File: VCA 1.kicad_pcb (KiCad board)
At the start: 2 copper layers, 171.3 x 128.5 mm, 89 parts, among them J1 Eurorack 2x8hs, J10 CV2, J11 IN2, J12 IN 1x8h, J13 OUT1, J14 OUT2, J15 IN 1x8s, J2 OUT 1x3s, J3 CV 1x9s, J5 CV 1x9h, J6 OUT 1x3h, J8 CV1, J9 IN1, Q1 2N3904, Q2 2N3904, U1 TL074, U2 AS2164

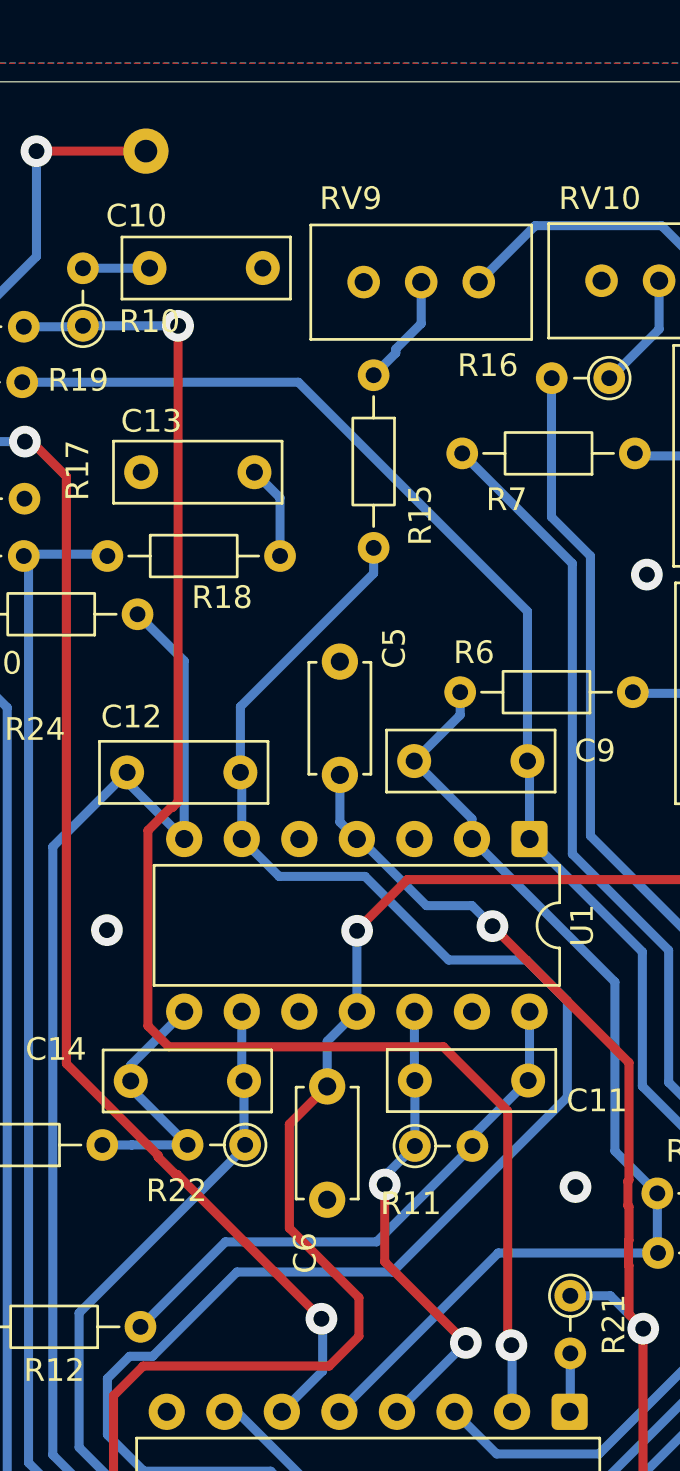
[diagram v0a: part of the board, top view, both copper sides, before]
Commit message: Added missing GND vias
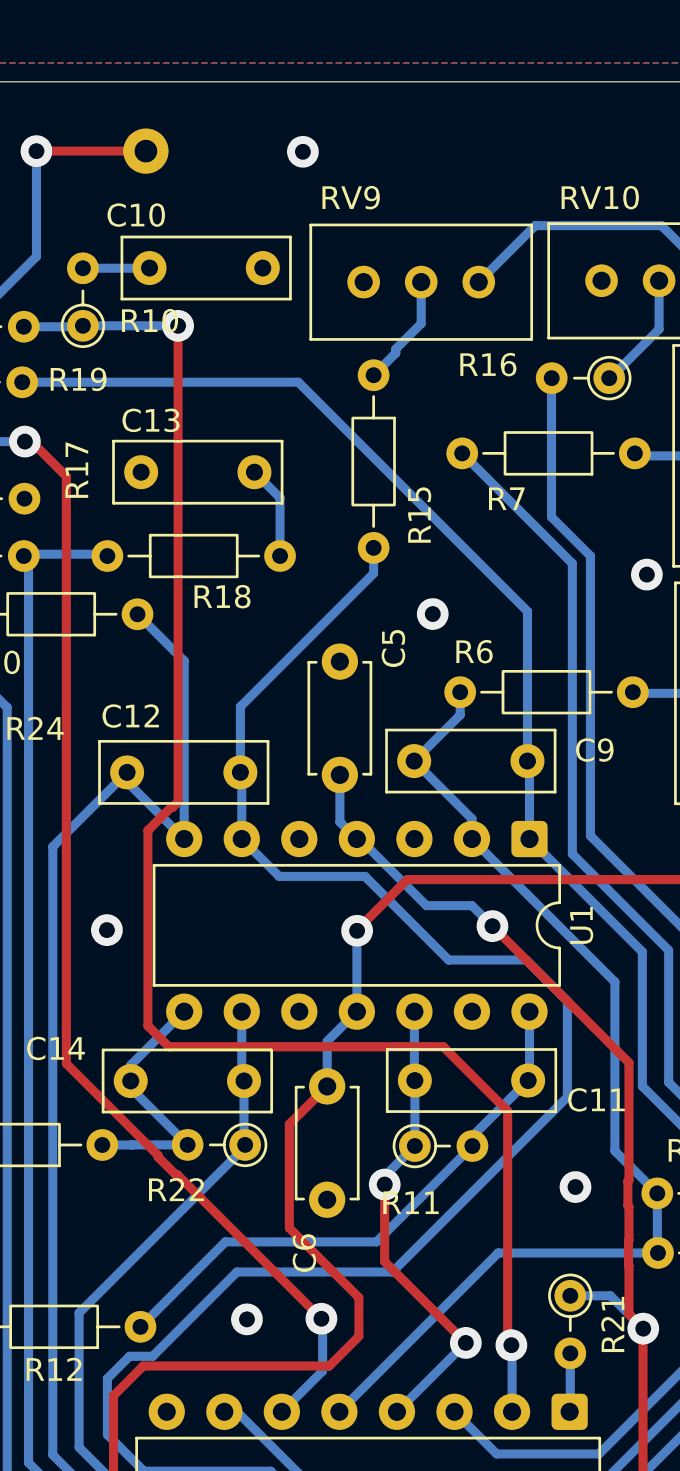
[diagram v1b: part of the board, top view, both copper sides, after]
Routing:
- net GND: vias 9 -> 12
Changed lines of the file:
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@@
+	)
+	(gr_circle
+		(center 44.15 87.07)
+		(end 45 87.07)
+		(stroke
+			(width 0.1)
+			(type default)
+		)
+		(fill yes)
+		(layer "F.Mask")
+	)
+	(gr_circle
+		(center 46.62 35.56)
+		(end 47.47 35.56)
+		(stroke
+			(width 0.1)
+			(type default)
+		)
+		(fill yes)
+		(layer "F.Mask")
 	)
 	(gr_circle
@@
 	)
 	(gr_circle
+		(center 52.34 55.93)
+		(end 53.19 55.93)
+		(stroke
+			(width 0.1)
+			(type default)
+		)
+		(fill yes)
+		(layer "F.Mask")
+	)
+	(gr_circle
 		(center 53.79 88.13)
 		(end 54.64 88.13)
@@
 	)
 	(gr_circle
+		(center 44.15 87.071199)
+		(end 45.008801 87.071199)
+		(stroke
+			(width 0.1)
+			(type default)
+		)
+		(fill yes)
+		(layer "B.Mask")
+	)
+	(gr_circle
+		(center 46.62 35.561199)
+		(end 47.478801 35.561199)
+		(stroke
+			(width 0.1)
+			(type default)
+		)
+		(fill yes)
+		(layer "B.Mask")
+	)
+	(gr_circle
 		(center 47.43 87.071199)
 		(end 48.288801 87.071199)
@@
 		(center 50.22 81.141199)
 		(end 51.078801 81.141199)
+		(stroke
+			(width 0.1)
+			(type default)
+		)
+		(fill yes)
+		(layer "B.Mask")
+	)
+	(gr_circle
+		(center 52.34 55.951199)
+		(end 53.198801 55.951199)
 		(stroke
 			(width 0.1)
@@
 	)
 	(via
+		(at 46.61 35.56)
+		(size 1.4)
+		(drill 0.7)
+		(layers "F.Cu" "B.Cu")
+		(free yes)
+		(net "GND")
+	)
+	(via
 		(at 102.79 51.82)
 		(size 1.4)
@@
 		(net "GND")
 	)
+	(via
+		(at 44.14 87.09)
+		(size 1.4)
+		(drill 0.7)
+		(layers "F.Cu" "B.Cu")
+		(free yes)
+		(net "GND")
+	)
+	(via
+		(at 52.34 55.96)
+		(size 1.4)
+		(drill 0.7)
+		(layers "F.Cu" "B.Cu")
+		(free yes)
+		(net "GND")
+	)

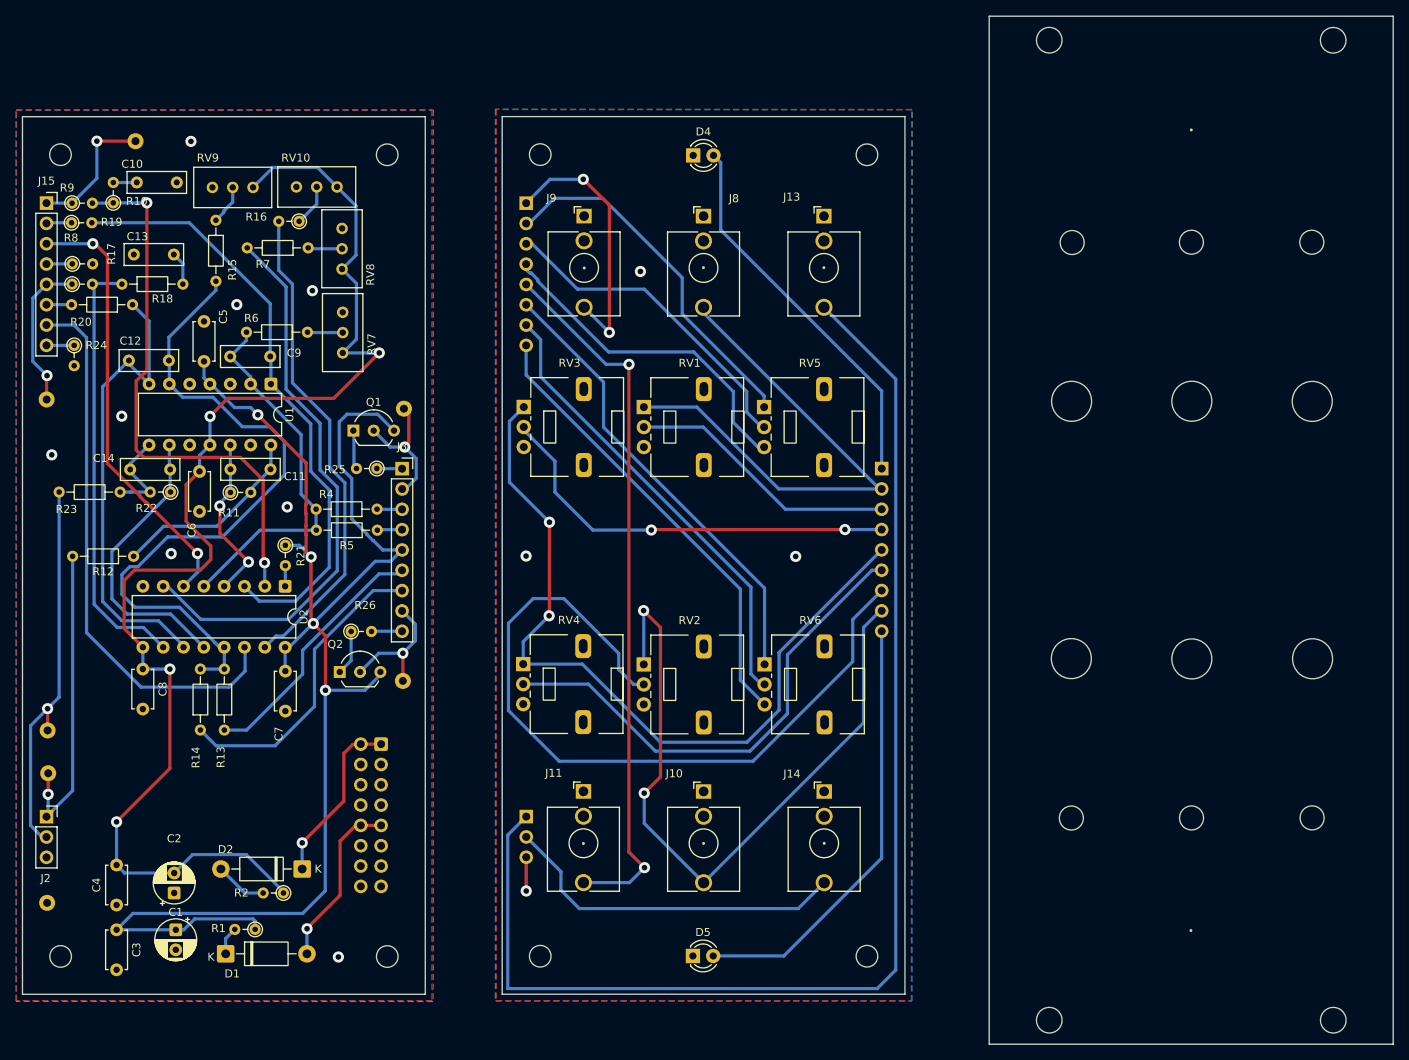
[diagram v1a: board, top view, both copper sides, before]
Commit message: Forgot panel pins are soldered on reverse
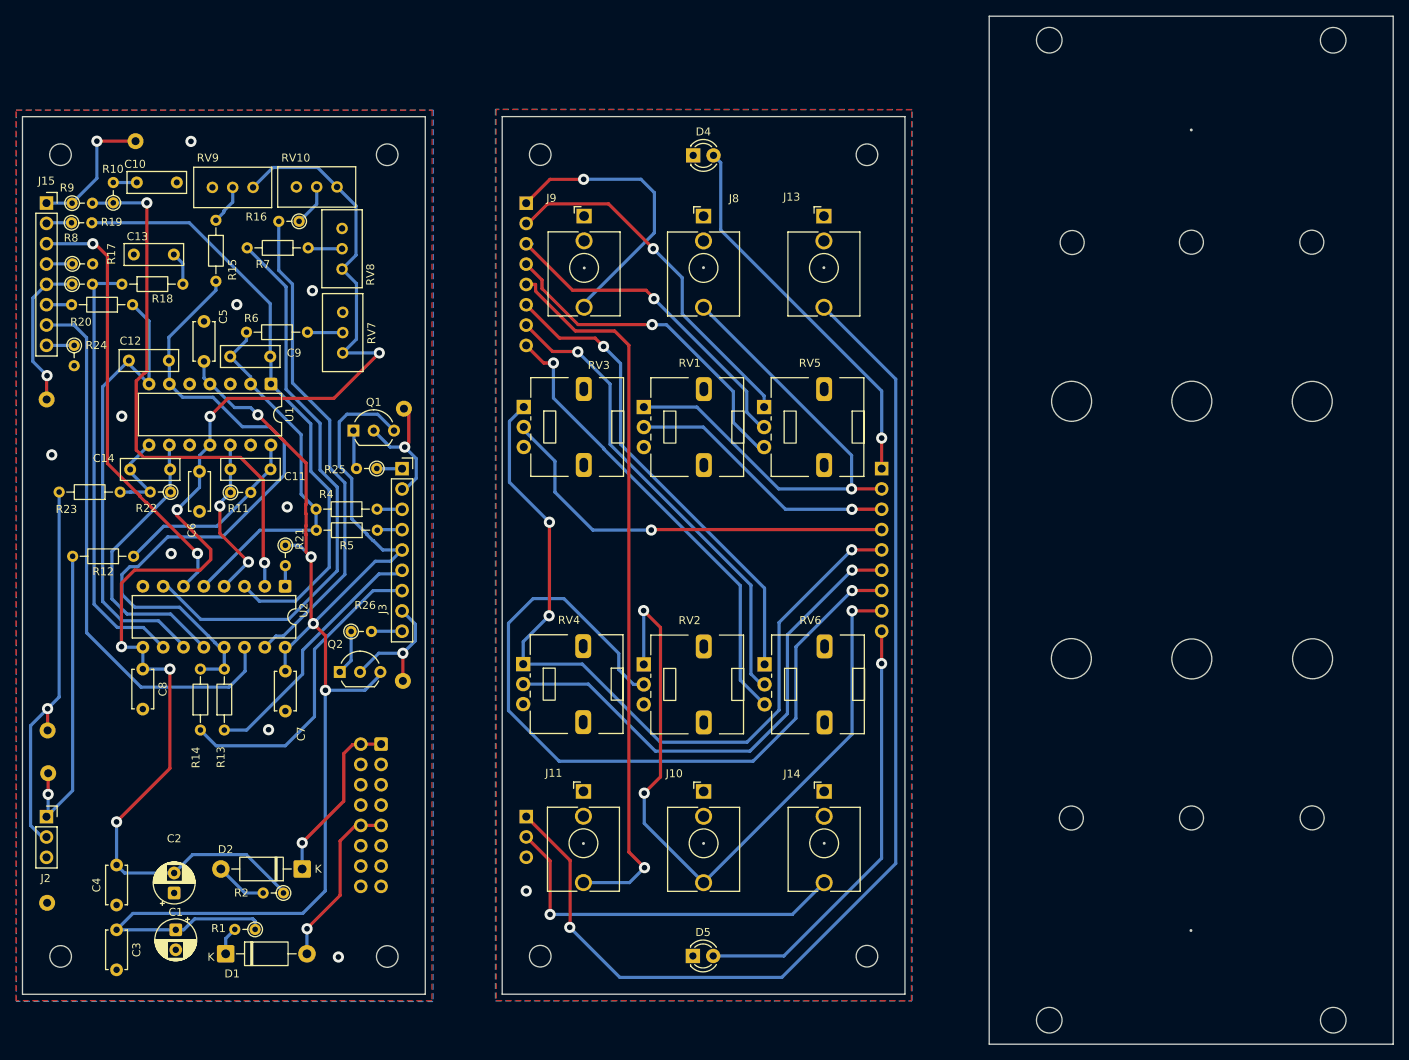
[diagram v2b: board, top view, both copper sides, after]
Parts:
- C7, C8: value 1μF c -> 0.1μF c
- R11, R22: value 10K -> 100K
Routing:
- net Net-(J6-Pin_1): track 158.5 -> 138.6 mm, vias 0 -> 1
- net GND: track 4.22 -> 0.00 mm, vias 12 -> 10
- net Net-(J6-Pin_2): track 43.7 -> 46.8 mm, vias 0 -> 1
- net -12V: track 186.6 -> 189.3 mm, vias 5 -> 7
- net Net-(J12-Pin_6): track 57.3 -> 59.9 mm, vias 0 -> 1
- net Net-(J12-Pin_1): track 33.3 -> 35.9 mm, vias 2 -> 1
- net Net-(J5-Pin_8): track 88.8 -> 91.1 mm, vias 2 -> 3
- net Net-(J5-Pin_5): track 99.4 -> 101.6 mm, vias 2 -> 3
- net Net-(J5-Pin_7): track 95.9 -> 98.1 mm, vias 0 -> 1
- net Net-(J12-Pin_5): track 89.1 -> 91.0 mm, vias 2 -> 1
- net Net-(J12-Pin_7): track 57.5 -> 59.3 mm, vias 0 -> 1
- net Net-(J5-Pin_6): track 62.0 -> 63.5 mm, vias 0 -> 1
- net Net-(J5-Pin_2): track 66.1 -> 65.0 mm, vias 0 -> 1
- net Net-(J12-Pin_3): track 40.8 -> 41.5 mm, vias 0 -> 1
- net Net-(J3-Pin_7): track 38.2 -> 39.0 mm
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
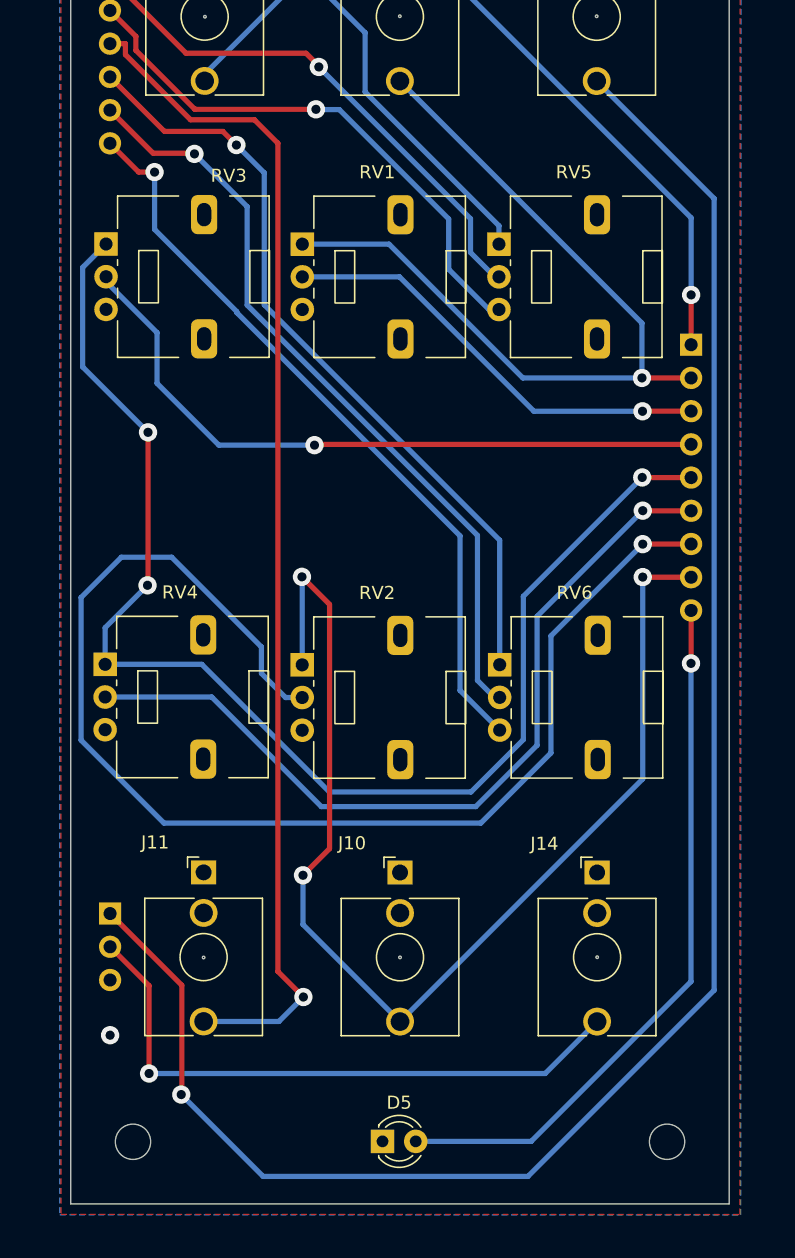
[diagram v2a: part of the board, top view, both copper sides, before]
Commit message: Updated panel layout and plots.
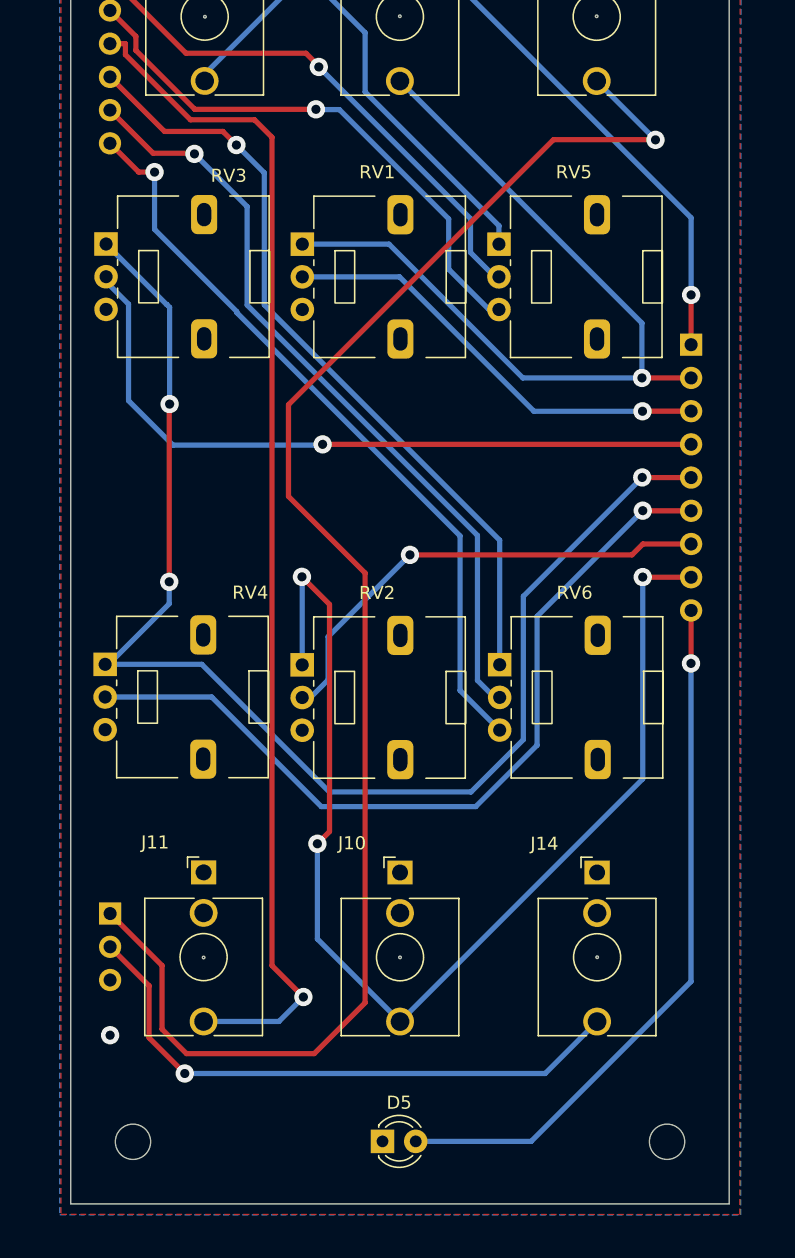
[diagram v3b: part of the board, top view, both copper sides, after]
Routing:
- net Net-(J5-Pin_7): track 98.1 -> 36.5 mm
- net Net-(J6-Pin_1): track 138.6 -> 119.3 mm
- net Net-(J5-Pin_4): track 52.6 -> 54.6 mm
- net Net-(J6-Pin_2): track 46.8 -> 45.2 mm
- net Net-(J5-Pin_8): track 91.1 -> 90.2 mm

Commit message: Updated controls and added licence
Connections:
- RV1 pad 1: Net-(J5-Pin_2) -> GND
- RV1 pad 3: GND -> Net-(J5-Pin_2)
- RV2 pad 1: Net-(J5-Pin_8) -> GND
- RV2 pad 3: GND -> Net-(J5-Pin_8)
- RV3 pad 1: Net-(J5-Pin_5) -> unconnected-(RV3-Pad1)
- RV3 pad 3: unconnected-(RV3-Pad3) -> Net-(J5-Pin_5)
- RV4 pad 1: Net-(J5-Pin_5) -> unconnected-(RV4-Pad1)
- RV4 pad 3: unconnected-(RV4-Pad3) -> Net-(J5-Pin_5)
- RV5 pad 1: Net-(J12-Pin_2) -> Net-(J12-Pin_4)
- RV5 pad 3: Net-(J12-Pin_4) -> Net-(J12-Pin_2)
- RV6 pad 1: Net-(J12-Pin_6) -> Net-(J12-Pin_8)
- RV6 pad 3: Net-(J12-Pin_8) -> Net-(J12-Pin_6)
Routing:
- net -12V: track 189.3 -> 209.2 mm
- net Net-(J5-Pin_5): track 101.6 -> 91.9 mm
- net Net-(J12-Pin_2): track 45.1 -> 54.7 mm
- net Net-(J5-Pin_8): track 90.2 -> 98.7 mm
- net Net-(J12-Pin_6): track 59.9 -> 67.5 mm
- net Net-(J5-Pin_4): track 54.6 -> 50.2 mm
- net Net-(J12-Pin_4): track 42.1 -> 37.8 mm
- net Net-(J12-Pin_3): track 41.5 -> 45.4 mm
- net Net-(U2-I_IN1): track 69.1 -> 72.0 mm
- net Net-(J5-Pin_2): track 65.0 -> 67.1 mm
- net Net-(C11-Pad2): track 24.9 -> 27.0 mm
- net Net-(U1B--): track 86.1 -> 87.6 mm
- net Net-(U1D-+): track 21.1 -> 22.6 mm
- net +12V: track 206.0 -> 207.3 mm
- net Net-(J12-Pin_8): track 57.9 -> 59.0 mm

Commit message: Updated versioning
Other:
- board text added: "Nigel Daniels - 2026 VCA 1 - Control V1.1"
- board text added: "Nigel Daniels 2026 VCA 1 - Main V 1.1"
- board text added: "V 1.1"
- board text removed: "V 1.0"

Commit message: Reoriented power and fixed flags
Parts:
- removed R19: 10K, Resistor_THT:R_Axial_DIN0204_L3.6mm_D1.6mm_P2.54mm_Vertical
- removed R20: 10K, Resistor_THT:R_Axial_DIN0204_L3.6mm_D1.6mm_P7.62mm_Horizontal
- R21: footprint Resistor_THT:R_Axial_DIN0204_L3.6mm_D1.6mm_P2.54mm_Vertical -> Resistor_THT:R_Axial_DIN0204_L3.6mm_D1.6mm_P7.62mm_Horizontal
- moved J1 17.9 mm to (67.9, 128.7), turned to 0 degrees
- moved D1 10.6 mm to (50.4, 126.5)
- moved D2 10.5 mm to (60.9, 137.0)
- moved R2 10.5 mm to (48.3, 133.0), turned to 0 degrees
- moved C4 7.86 mm to (37.8, 138.9)
- moved R1 7.78 mm to (48.1, 129.8), turned to 0 degrees
- moved C2 7.74 mm to (44.0, 137.2)
- moved R21 6.19 mm to (58.3, 79.9)
- moved C1 5.87 mm to (44.2, 128.3), turned to 90 degrees
- moved C3 5.05 mm to (37.8, 129.1), turned to 90 degrees
- moved C12 0.19 mm to (43.7, 62.8)
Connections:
- C1 pad 1: +12V -> +12v
- C12 pad 2: Net-(U2-VC3) -> Net-(J15-Pin_6)
- C2 pad 2: -12V -> -12v
- C3 pad 1: +12V -> +12v
- C4 pad 2: -12V -> -12v
- C5 pad 1: +12V -> +12v
- C6 pad 2: -12V -> -12v
- C7 pad 1: +12V -> +12v
- C8 pad 1: -12V -> -12v
- C9 pad 2: Net-(U2-VC1) -> Net-(J15-Pin_2)
- J3 pad 5: +12V -> +12v
- Q1 pad 3: +12V -> +12v
- Q2 pad 3: +12V -> +12v
- R1 pad 1: +12V -> +12v
- R2 pad 1: -12V -> -12v
- R21 pad 1: +12V -> +12v
- RV10 pad 1: -12V -> -12v
- RV7 pad 1: -12V -> -12v
- RV8 pad 1: -12V -> -12v
- RV9 pad 1: -12V -> -12v
- U1 pad 1: Net-(U2-VC1) -> Net-(J15-Pin_2)
- U1 pad 11: -12V -> -12v
- U1 pad 4: +12V -> +12v
- U1 pad 7: Net-(U2-VC3) -> Net-(J15-Pin_6)
- U2 pad 11: Net-(U2-VC3) -> Net-(J15-Pin_6)
- U2 pad 16: +12V -> +12v
- U2 pad 3: Net-(U2-VC1) -> Net-(J15-Pin_2)
- U2 pad 9: -12V -> -12v
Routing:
- net -12V: track 209.2 -> 14.8 mm, vias 7 -> 1
- net +12V: track 207.3 -> 15.1 mm, vias 5 -> 1
- net -12v: track 0.00 -> 185.4 mm, vias 0 -> 6
- net +12v: track 0.00 -> 159.1 mm, vias 0 -> 3
- net Net-(J15-Pin_2): track 3.16 -> 81.4 mm
- net Net-(U2-VC1): track 75.7 -> 0.00 mm
- net Net-(J15-Pin_6): track 3.14 -> 63.3 mm, vias 0 -> 2
- net Net-(U2-VC3): track 58.8 -> 0.00 mm
- net Net-(J15-Pin_3): track 55.4 -> 58.4 mm
- net Net-(J3-Pin_6): track 32.2 -> 35.3 mm
- net Net-(D2-A): track 6.52 -> 4.03 mm
- net Net-(U2-MODE): track 2.59 -> 3.71 mm
- net GND: vias 10 -> 9
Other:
- board text added: "Nigel Daniels - 2026 VCA 1 - Control V1.2"
- board text added: "Nigel Daniels 2026 VCA 1 - Main V 1.2"
- board text added: "V 1.2"
- board text removed: "Nigel Daniels - 2026 VCA 1 - Control V1.1"
- board text removed: "Nigel Daniels 2026 VCA 1 - Main V 1.1"
- board text removed: "V 1.1"

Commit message: Updated versioning
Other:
- board text added: "Nigel Daniels - 2026 VCA 1 - Control V1.3"
- board text added: "Nigel Daniels 2026 VCA 1 - Main V 1.3"
- board text added: "V 1.3"
- board text removed: "Nigel Daniels - 2026 VCA 1 - Control V1.2"
- board text removed: "Nigel Daniels 2026 VCA 1 - Main V 1.2"
- board text removed: "V 1.2"
